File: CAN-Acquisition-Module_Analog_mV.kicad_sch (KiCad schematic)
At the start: 33 parts

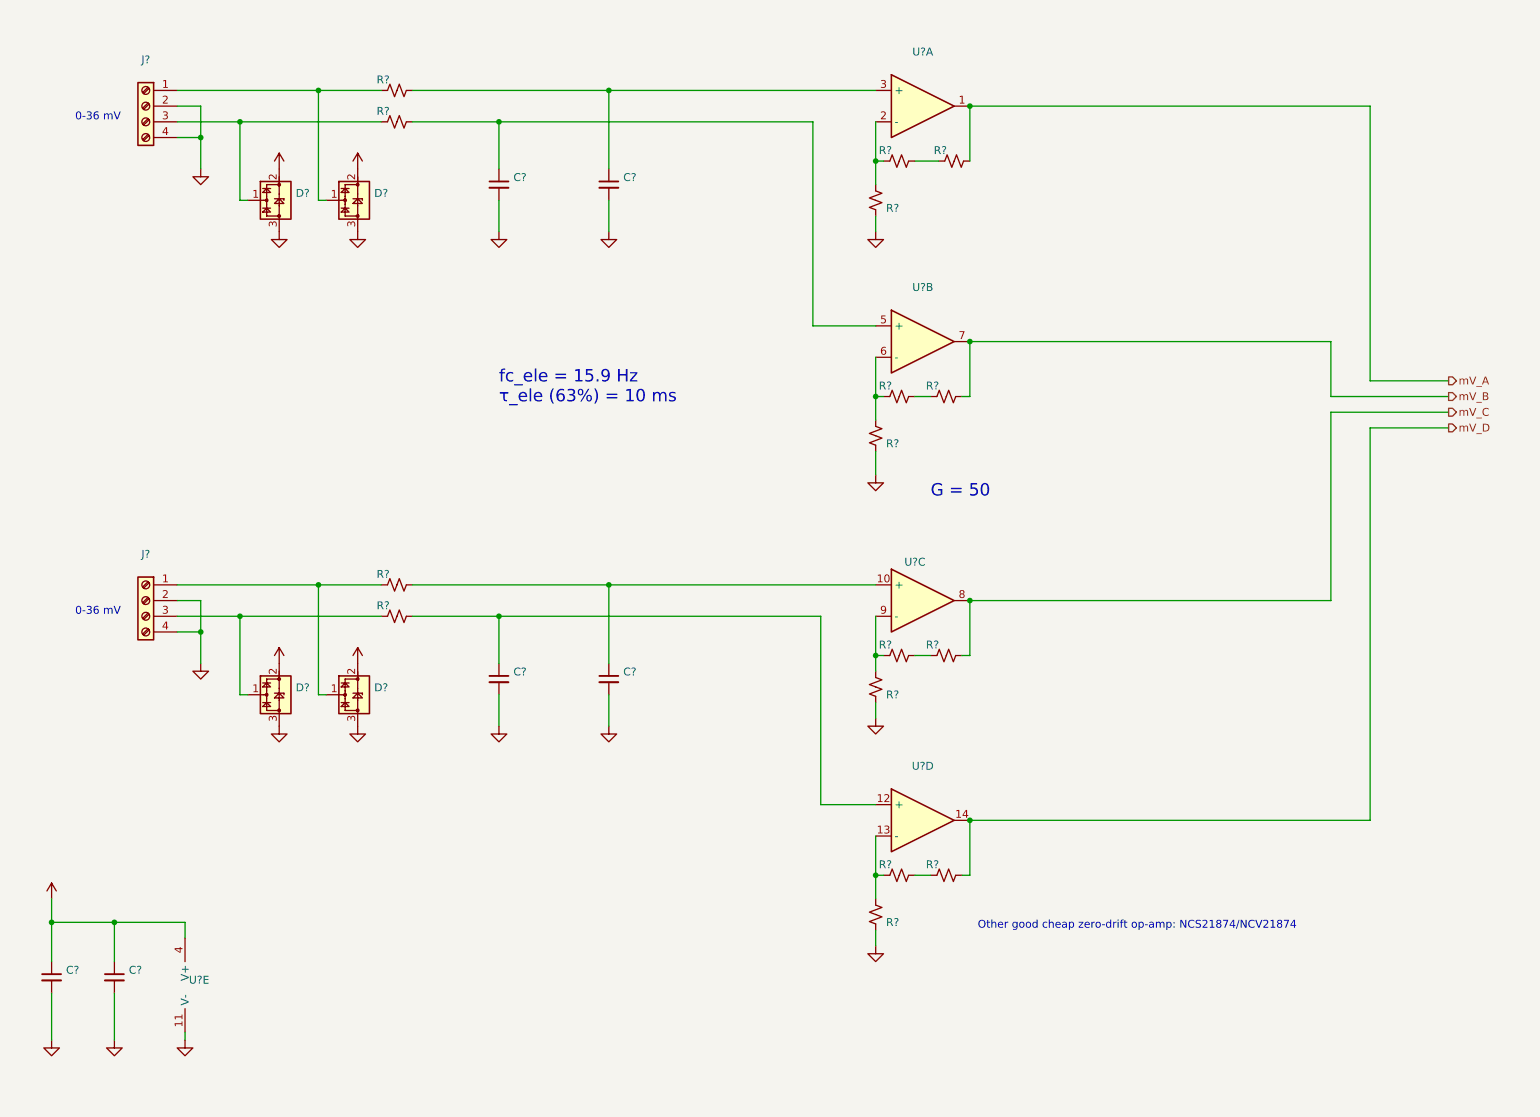
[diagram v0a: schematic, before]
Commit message: Added screen sections and annotations
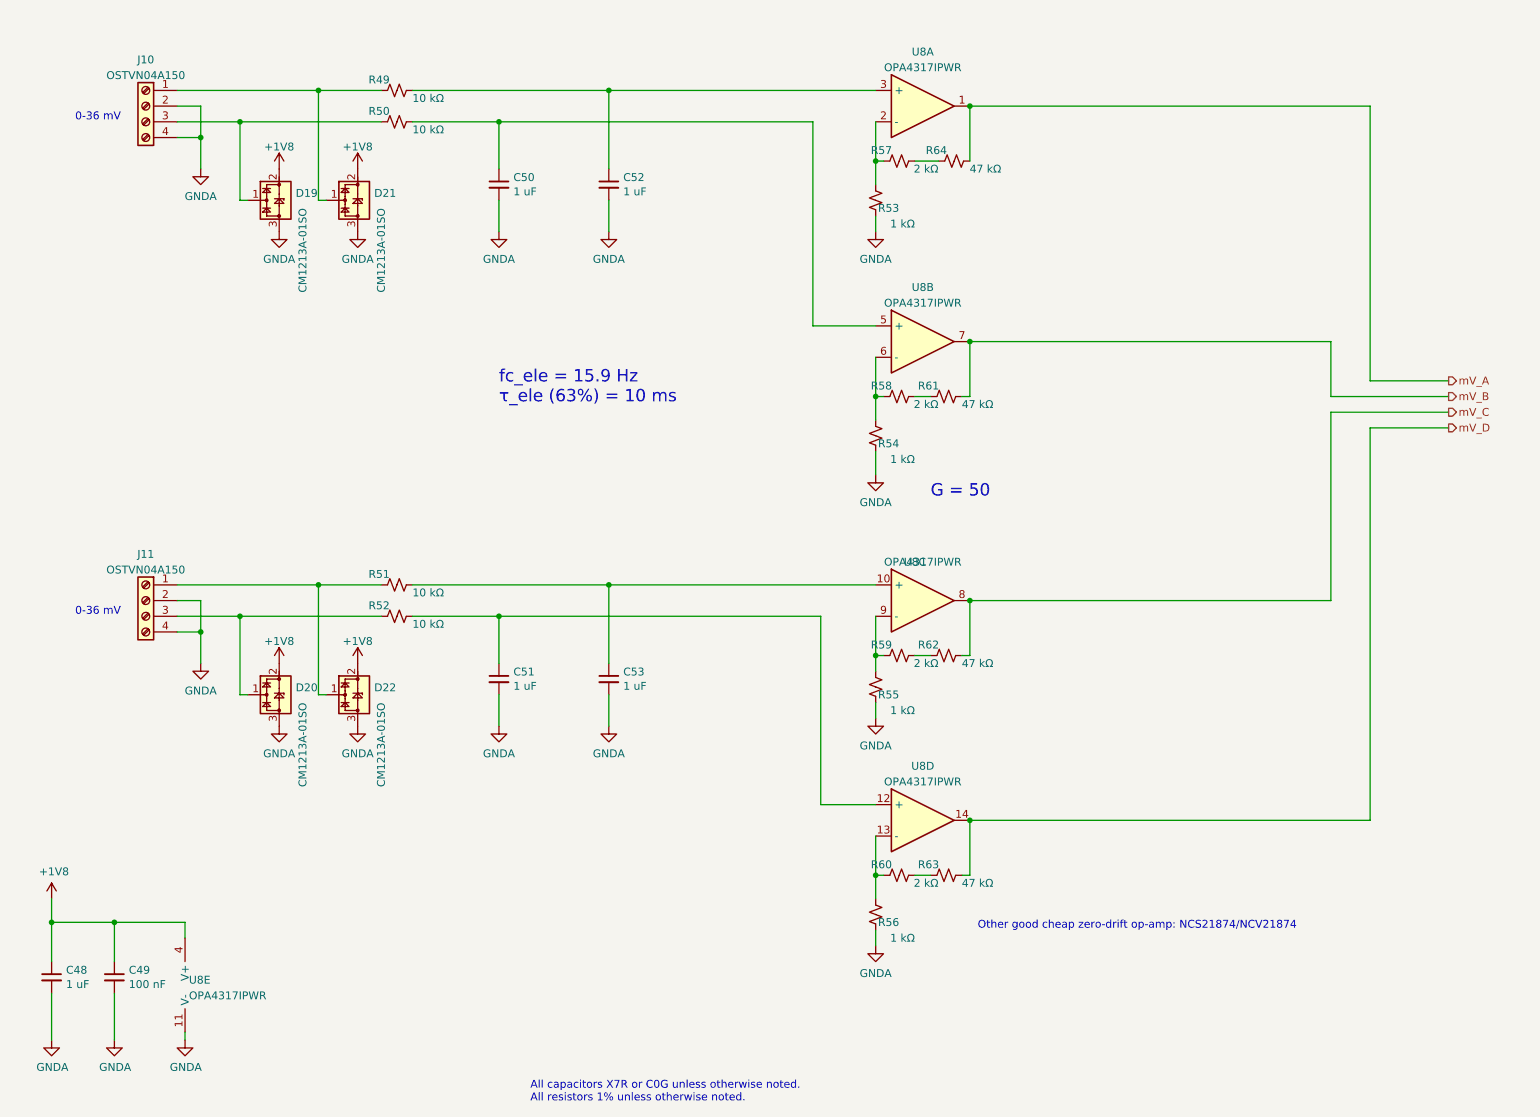
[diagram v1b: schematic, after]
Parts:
- C48, C50, C51, C52, C53: renamed from C?; value (none) -> 1 uF; footprint (none) -> Capacitor_SMD:C_0603_1608Metric; Mfr. (none) -> Samsung Electro-Mechanics; P/N (none) -> CL10B105KA8NNNC; Rated Voltage (none) -> 25V
- C49: renamed from C?; value (none) -> 100 nF; footprint (none) -> Capacitor_SMD:C_0402_1005Metric; Mfr. (none) -> KYOCERA AVX; P/N (none) -> 0402YC104KAT2A; Rated Voltage (none) -> 16V
- D19, D20, D21, D22: renamed from D?; value (none) -> CM1213A-01SO; footprint (none) -> Package_TO_SOT_SMD:SOT-23
- J10, J11: renamed from J?; value (none) -> OSTVN04A150; footprint (none) -> CAN-Acquisition-Module:OSTVN04A150; P/N (none) -> OSTVN04A150
- R49, R50, R51, R52: renamed from R?; value (none) -> 10 kΩ; footprint (none) -> Resistor_SMD:R_0603_1608Metric
- R53, R54, R55, R56: renamed from R?; value (none) -> 1 kΩ; footprint (none) -> Resistor_SMD:R_0603_1608Metric
- R57, R58, R59, R60: renamed from R?; value (none) -> 2 kΩ; footprint (none) -> Resistor_SMD:R_0603_1608Metric
- R61, R62, R63, R64: renamed from R?; value (none) -> 47 kΩ; footprint (none) -> Resistor_SMD:R_0603_1608Metric
- U8: renamed from U?; value (none) -> OPA4317IPWR; footprint (none) -> Package_SO:TSSOP-14_4.4x5mm_P0.65mm
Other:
- note added: "All capacitors X7R or C0G unless otherwise noted. All resistors 1% unless otherwise noted."

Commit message: PCB started
Placement well advanced
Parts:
- added R75, R76, R77, R78: Ω, Resistor_SMD:R_0603_1608Metric, symbol Device:R_Small_US
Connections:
- net GNDA: now also R75.2, R76.2, R77.2, R78.2
- net mV_A: now also U8.7; no longer U8.1
- net mV_B: now also U8.1; no longer U8.7
- net mV_C: now also U8.14; no longer U8.8
- net mV_D: now also U8.8; no longer U8.14
- net at C53.1, R51.2: now also U8.12 (+), R78.1; no longer U8.10 (+)
- net at R53.2, R57.1: now also U8.6 (-); no longer U8.2 (-)
- net at C52.1, R49.2: now also U8.5 (+), R77.1; no longer U8.3 (+)
- net at R54.2, R58.1: now also U8.2 (-); no longer U8.6 (-)
- net at R55.2, R59.1: now also U8.13 (-); no longer U8.9 (-)
- net at C50.1, R50.2: now also U8.3 (+), R75.1; no longer U8.5 (+)
- net at C51.1, R52.2: now also U8.10 (+), R76.1; no longer U8.12 (+)
- net at R56.2, R60.1: now also U8.9 (-); no longer U8.13 (-)
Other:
- moved on the sheet: C50, C51, C52, C53, U8A, U8B, U8C, U8D

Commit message: Layout of analog section started
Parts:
- added C52, C53: 100 nF, Capacitor_SMD:C_0402_1005Metric, symbol Device:C_Small
- renumbered C48 to C50, C49 to C51, C50 to C54, C51 to C55, C52 to C56, C53 to C57, R75 to R53, R76 to R54, R77 to R55, R78 to R56, R53 to R57, R54 to R58, R55 to R59, R56 to R60, R57 to R61, R58 to R62, R59 to R63, R60 to R64, R61 to R65, R62 to R66, R63 to R67, R64 to R68
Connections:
- net +1V8: now also C52.1, C53.1
- net GNDA: now also C52.2, C53.2

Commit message: Analog section, screen and USB finished
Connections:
- net mV_A: now also U8.1; no longer U8.7
- net mV_B: now also U8.7; no longer U8.1
- net mV_C: now also U8.8; no longer U8.14
- net mV_D: now also U8.14; no longer U8.8
- net at C57.1, R51.2, R56.1: now also U8.10 (+); no longer U8.12 (+)
- net at R58.2, R62.1: now also U8.6 (-); no longer U8.2 (-)
- net at C54.1, R50.2, R53.1: now also U8.5 (+); no longer U8.3 (+)
- net at C56.1, R49.2, R55.1: now also U8.3 (+); no longer U8.5 (+)
- net at R59.2, R63.1: now also U8.9 (-); no longer U8.13 (-)
- net at C55.1, R52.2, R54.1: now also U8.12 (+); no longer U8.10 (+)
- net at R57.2, R61.1: now also U8.2 (-); no longer U8.6 (-)
- net at R60.2, R64.1: now also U8.13 (-); no longer U8.9 (-)
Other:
- moved on the sheet: U8A, U8B, U8C, U8D
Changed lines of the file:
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@@
     (comment 1 "Designer: Hugo Boyce")
   )
+  (junction (at 58.42 34.29) (diameter 0) (color 0 0 0 0)
+  )
+  (junction (at 106.68 114.3) (diameter 0) (color 0 0 0 0)
+  )
+  (junction (at 176.53 147.32) (diameter 0) (color 0 0 0 0)
+  )
+  (junction (at 176.53 69.85) (diameter 0) (color 0 0 0 0)
+  )
+  (junction (at 58.42 114.3) (diameter 0) (color 0 0 0 0)
+  )
+  (junction (at 123.19 29.21) (diameter 0) (color 0 0 0 0)
+  )
   (junction (at 176.53 31.75) (diameter 0) (color 0 0 0 0)
   )
-  (junction (at 58.42 34.29) (diameter 0) (color 0 0 0 0)
-  )
-  (junction (at 106.68 114.3) (diameter 0) (color 0 0 0 0)
-  )
-  (junction (at 58.42 114.3) (diameter 0) (color 0 0 0 0)
-  )
-  (junction (at 123.19 29.21) (diameter 0) (color 0 0 0 0)
-  )
   (junction (at 161.29 156.21) (diameter 0) (color 0 0 0 0)
   )
@@
   (junction (at 71.12 109.22) (diameter 0) (color 0 0 0 0)
   )
-  (junction (at 176.53 69.85) (diameter 0) (color 0 0 0 0)
-  )
   (junction (at 132.08 109.22) (diameter 0) (color 0 0 0 0)
   )
+  (junction (at 176.53 111.76) (diameter 0) (color 0 0 0 0)
+  )
   (junction (at 27.94 163.83) (diameter 0) (color 0 0 0 0)
   )
@@
   )
   (junction (at 38.1 163.83) (diameter 0) (color 0 0 0 0)
-  )
-  (junction (at 176.53 111.76) (diameter 0) (color 0 0 0 0)
-  )
-  (junction (at 176.53 147.32) (diameter 0) (color 0 0 0 0)
   )
   (junction (at 106.68 34.29) (diameter 0) (color 0 0 0 0)
@@
     (pin "1")
   )
-  (symbol (lib_id "Amplifier_Operational:OPA4196xPW") (at 168.91 69.85 0) (unit 1)
-    (in_bom yes) (on_board yes) (fields_autoplaced)
-    (property "Reference" "U8" (id 0) (at 168.91 61.0702 0))
-    (property "Value" "OPA4317IPWR" (id 1) (at 168.91 63.6071 0))
-    (property "Footprint" "Package_SO:TSSOP-14_4.4x5mm_P0.65mm" (id 2) (at 168.91 69.85 0)
-      (effects (font (size 1.27 1.27)) hide)
-    )
-    (property "Datasheet" "https://www.ti.com/general/docs/suppproductinfo.tsp?distId=10&gotoUrl=https%3A%2F%2Fwww.ti.com%2Flit%2Fgpn%2Fopa4317" (id 3) (at 168.91 69.85 0)
+  (symbol (lib_id "Amplifier_Operational:OPA4196xPW") (at 168.91 31.75 0) (unit 1)
+    (in_bom yes) (on_board yes) (fields_autoplaced)
+    (property "Reference" "U8" (id 0) (at 168.91 22.9702 0))
+    (property "Value" "OPA4317IPWR" (id 1) (at 168.91 25.5071 0))
+    (property "Footprint" "Package_SO:TSSOP-14_4.4x5mm_P0.65mm" (id 2) (at 168.91 31.75 0)
+      (effects (font (size 1.27 1.27)) hide)
+    )
+    (property "Datasheet" "https://www.ti.com/general/docs/suppproductinfo.tsp?distId=10&gotoUrl=https%3A%2F%2Fwww.ti.com%2Flit%2Fgpn%2Fopa4317" (id 3) (at 168.91 31.75 0)
       (effects (font (size 1.27 1.27)) hide)
     )
@@
     (pin "2")
   )
-  (symbol (lib_id "Amplifier_Operational:OPA4196xPW") (at 168.91 147.32 0) (unit 3)
-    (in_bom yes) (on_board yes)
-    (property "Reference" "U8" (id 0) (at 167.64 141.0802 0))
-    (property "Value" "OPA4317IPWR" (id 1) (at 168.91 141.0771 0))
-    (property "Footprint" "Package_SO:TSSOP-14_4.4x5mm_P0.65mm" (id 2) (at 168.91 147.32 0)
-      (effects (font (size 1.27 1.27)) hide)
-    )
-    (property "Datasheet" "https://www.ti.com/general/docs/suppproductinfo.tsp?distId=10&gotoUrl=https%3A%2F%2Fwww.ti.com%2Flit%2Fgpn%2Fopa4317" (id 3) (at 168.91 147.32 0)
+  (symbol (lib_id "Amplifier_Operational:OPA4196xPW") (at 168.91 111.76 0) (unit 3)
+    (in_bom yes) (on_board yes)
+    (property "Reference" "U8" (id 0) (at 167.64 105.5202 0))
+    (property "Value" "OPA4317IPWR" (id 1) (at 168.91 105.5171 0))
+    (property "Footprint" "Package_SO:TSSOP-14_4.4x5mm_P0.65mm" (id 2) (at 168.91 111.76 0)
+      (effects (font (size 1.27 1.27)) hide)
+    )
+    (property "Datasheet" "https://www.ti.com/general/docs/suppproductinfo.tsp?distId=10&gotoUrl=https%3A%2F%2Fwww.ti.com%2Flit%2Fgpn%2Fopa4317" (id 3) (at 168.91 111.76 0)
       (effects (font (size 1.27 1.27)) hide)
     )
@@
     (pin "4")
   )
-  (symbol (lib_id "Amplifier_Operational:OPA4196xPW") (at 168.91 111.76 0) (unit 4)
-    (in_bom yes) (on_board yes) (fields_autoplaced)
-    (property "Reference" "U8" (id 0) (at 168.91 102.9802 0))
-    (property "Value" "OPA4317IPWR" (id 1) (at 168.91 105.5171 0))
-    (property "Footprint" "Package_SO:TSSOP-14_4.4x5mm_P0.65mm" (id 2) (at 168.91 111.76 0)
-      (effects (font (size 1.27 1.27)) hide)
-    )
-    (property "Datasheet" "https://www.ti.com/general/docs/suppproductinfo.tsp?distId=10&gotoUrl=https%3A%2F%2Fwww.ti.com%2Flit%2Fgpn%2Fopa4317" (id 3) (at 168.91 111.76 0)
+  (symbol (lib_id "Amplifier_Operational:OPA4196xPW") (at 168.91 147.32 0) (unit 4)
+    (in_bom yes) (on_board yes) (fields_autoplaced)
+    (property "Reference" "U8" (id 0) (at 168.91 138.5402 0))
+    (property "Value" "OPA4317IPWR" (id 1) (at 168.91 141.0771 0))
+    (property "Footprint" "Package_SO:TSSOP-14_4.4x5mm_P0.65mm" (id 2) (at 168.91 147.32 0)
+      (effects (font (size 1.27 1.27)) hide)
+    )
+    (property "Datasheet" "https://www.ti.com/general/docs/suppproductinfo.tsp?distId=10&gotoUrl=https%3A%2F%2Fwww.ti.com%2Flit%2Fgpn%2Fopa4317" (id 3) (at 168.91 147.32 0)
       (effects (font (size 1.27 1.27)) hide)
     )
@@
     (pin "1")
   )
-  (symbol (lib_id "Amplifier_Operational:OPA4196xPW") (at 168.91 31.75 0) (unit 2)
-    (in_bom yes) (on_board yes) (fields_autoplaced)
-    (property "Reference" "U8" (id 0) (at 168.91 22.9702 0))
-    (property "Value" "OPA4317IPWR" (id 1) (at 168.91 25.5071 0))
-    (property "Footprint" "Package_SO:TSSOP-14_4.4x5mm_P0.65mm" (id 2) (at 168.91 31.75 0)
-      (effects (font (size 1.27 1.27)) hide)
-    )
-    (property "Datasheet" "https://www.ti.com/general/docs/suppproductinfo.tsp?distId=10&gotoUrl=https%3A%2F%2Fwww.ti.com%2Flit%2Fgpn%2Fopa4317" (id 3) (at 168.91 31.75 0)
-      (effects (font (size 1.27 1.27)) hide)
-    )
+  (symbol (lib_id "Amplifier_Operational:OPA4196xPW") (at 168.91 69.85 0) (unit 2)
+    (in_bom yes) (on_board yes) (fields_autoplaced)
+    (property "Reference" "U8" (id 0) (at 168.91 61.0702 0))
+    (property "Value" "OPA4317IPWR" (id 1) (at 168.91 63.6071 0))
+    (property "Footprint" "Package_SO:TSSOP-14_4.4x5mm_P0.65mm" (id 2) (at 168.91 69.85 0)
+      (effects (font (size 1.27 1.27)) hide)
+    )
+    (property "Datasheet" "https://www.ti.com/general/docs/suppproductinfo.tsp?distId=10&gotoUrl=https%3A%2F%2Fwww.ti.com%2Flit%2Fgpn%2Fopa4317" (id 3) (at 168.91 69.85 0)
+      (effects (font (size 1.27 1.27)) hide)
+    )

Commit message: Finished power outputs
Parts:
- renumbered C50 to C49, C51 to C50, C52 to C51, C53 to C52, C54 to C53, C55 to C54, C56 to C55, C57 to C56, D19 to D21, D20 to D22, D21 to D23, D22 to D24, R49 to R50, R50 to R51, R51 to R52, R52 to R53, R53 to R54, R54 to R55, R55 to R56, R56 to R57, R57 to R58, R58 to R59, R59 to R60, R60 to R61, R61 to R62, R62 to R63, R63 to R64, R64 to R65, R65 to R66, R66 to R67, R67 to R68, R68 to R69

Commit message: forgor to save
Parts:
- renumbered C49 to C50, C50 to C51, C51 to C52, C52 to C53, C53 to C54, C54 to C55, C55 to C56, C56 to C57

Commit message: Rev. A1 release
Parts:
- renumbered C50 to C51, C51 to C52, C52 to C53, C53 to C54, C54 to C55, C55 to C56, C56 to C57, C57 to C58, R50 to R52, R51 to R53, R52 to R54, R53 to R55, R54 to R56, R55 to R57, R56 to R58, R57 to R59, R58 to R60, R59 to R61, R60 to R62, R61 to R63, R62 to R64, R63 to R65, R64 to R66, R65 to R67, R66 to R68, R67 to R69, R68 to R70, R69 to R71, U8 to U9
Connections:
- net mV_A: now also R68.2, U9.7; no longer R71.2, U9.1
- net mV_B: now also R71.2, U9.1; no longer R68.2, U9.7
- net mV_C: now also R70.2, U9.14; no longer R69.2, U9.8
- net mV_D: now also R69.2, U9.8; no longer R70.2, U9.14
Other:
- moved on the sheet: C53, C54, C55, C56, C57, C58, D21, D22, D23, D24, J10, J11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
